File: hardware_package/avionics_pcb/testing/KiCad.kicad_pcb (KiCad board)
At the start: 2 copper layers, 13.3 x 14.6 mm, 4 parts, among them J1 Conn_01x04, U1 AD8603

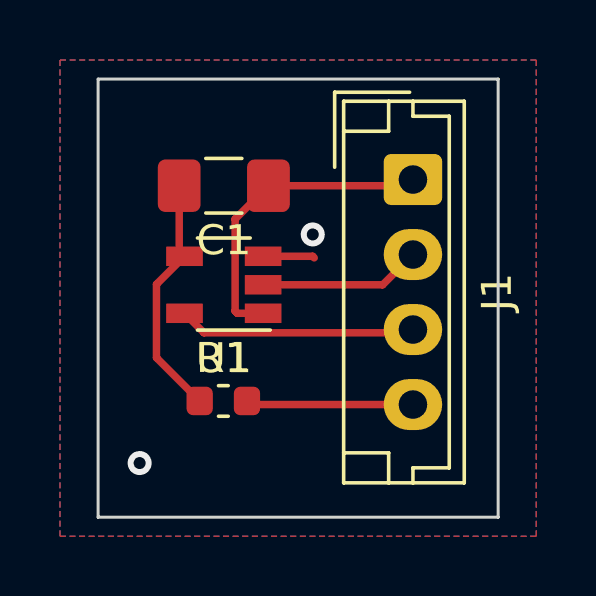
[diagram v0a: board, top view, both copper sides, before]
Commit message: disconnected pad from PCB, testing if the pipeline works correctly
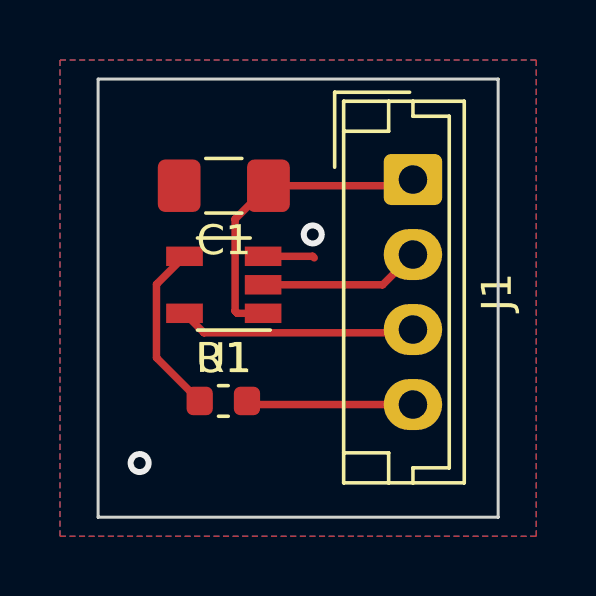
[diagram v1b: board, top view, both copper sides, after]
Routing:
- net Net-(C1-Pad2): track 8.23 -> 6.06 mm

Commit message: Connected pad to PCB, testing if the pipeline works correctly
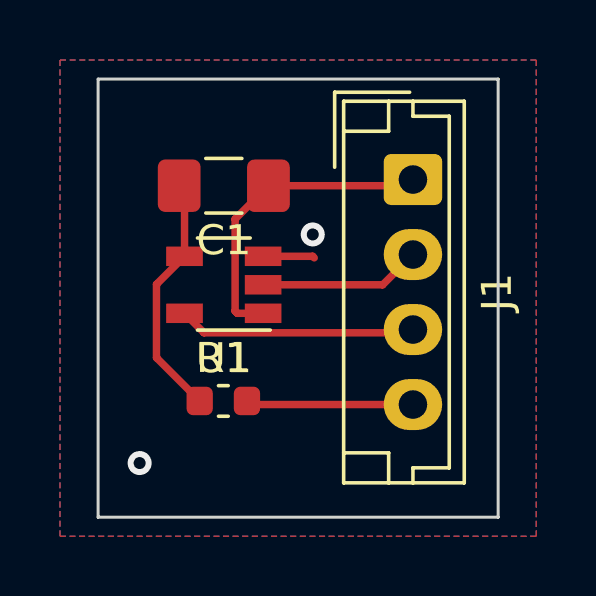
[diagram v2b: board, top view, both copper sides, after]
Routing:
- net Net-(C1-Pad2): track 6.06 -> 8.48 mm
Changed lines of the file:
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@@
     (thickness 1.6)
     (drawings 4)
-    (tracks 22)
+    (tracks 24)
     (zones 0)
     (modules 4)
@@
       (effects (font (size 0.5 0.5) (thickness 0.125)))
     )
+    (fp_line (start -1.6 0.8) (end -1.6 -0.8) (layer F.Fab) (width 0.1))
+    (fp_line (start -1.6 -0.8) (end 1.6 -0.8) (layer F.Fab) (width 0.1))
+    (fp_line (start 1.6 -0.8) (end 1.6 0.8) (layer F.Fab) (width 0.1))
+    (fp_line (start 1.6 0.8) (end -1.6 0.8) (layer F.Fab) (width 0.1))
+    (fp_line (start -0.602064 -0.91) (end 0.602064 -0.91) (layer F.SilkS) (width 0.12))
+    (fp_line (start -0.602064 0.91) (end 0.602064 0.91) (layer F.SilkS) (width 0.12))
+    (fp_line (start -2.45 1.12) (end -2.45 -1.12) (layer F.CrtYd) (width 0.05))
+    (fp_line (start -2.45 -1.12) (end 2.45 -1.12) (layer F.CrtYd) (width 0.05))
+    (fp_line (start 2.45 -1.12) (end 2.45 1.12) (layer F.CrtYd) (width 0.05))
     (fp_line (start 2.45 1.12) (end -2.45 1.12) (layer F.CrtYd) (width 0.05))
-    (fp_line (start 2.45 -1.12) (end 2.45 1.12) (layer F.CrtYd) (width 0.05))
-    (fp_line (start -2.45 -1.12) (end 2.45 -1.12) (layer F.CrtYd) (width 0.05))
-    (fp_line (start -2.45 1.12) (end -2.45 -1.12) (layer F.CrtYd) (width 0.05))
-    (fp_line (start -0.602064 0.91) (end 0.602064 0.91) (layer F.SilkS) (width 0.12))
-    (fp_line (start -0.602064 -0.91) (end 0.602064 -0.91) (layer F.SilkS) (width 0.12))
-    (fp_line (start 1.6 0.8) (end -1.6 0.8) (layer F.Fab) (width 0.1))
-    (fp_line (start 1.6 -0.8) (end 1.6 0.8) (layer F.Fab) (width 0.1))
-    (fp_line (start -1.6 -0.8) (end 1.6 -0.8) (layer F.Fab) (width 0.1))
-    (fp_line (start -1.6 0.8) (end -1.6 -0.8) (layer F.Fab) (width 0.1))
     (fp_text user %R (at 0 0) (layer F.Fab)
       (effects (font (size 0.8 0.8) (thickness 0.12)))
@@
       (effects (font (size 0.5 0.5) (thickness 0.125)))
     )
+    (fp_line (start -0.8 0.4) (end -0.8 -0.4) (layer F.Fab) (width 0.1))
+    (fp_line (start -0.8 -0.4) (end 0.8 -0.4) (layer F.Fab) (width 0.1))
+    (fp_line (start 0.8 -0.4) (end 0.8 0.4) (layer F.Fab) (width 0.1))
+    (fp_line (start 0.8 0.4) (end -0.8 0.4) (layer F.Fab) (width 0.1))
+    (fp_line (start -0.162779 -0.51) (end 0.162779 -0.51) (layer F.SilkS) (width 0.12))
+    (fp_line (start -0.162779 0.51) (end 0.162779 0.51) (layer F.SilkS) (width 0.12))
+    (fp_line (start -1.48 0.73) (end -1.48 -0.73) (layer F.CrtYd) (width 0.05))
+    (fp_line (start -1.48 -0.73) (end 1.48 -0.73) (layer F.CrtYd) (width 0.05))
+    (fp_line (start 1.48 -0.73) (end 1.48 0.73) (layer F.CrtYd) (width 0.05))
     (fp_line (start 1.48 0.73) (end -1.48 0.73) (layer F.CrtYd) (width 0.05))
-    (fp_line (start 1.48 -0.73) (end 1.48 0.73) (layer F.CrtYd) (width 0.05))
-    (fp_line (start -1.48 -0.73) (end 1.48 -0.73) (layer F.CrtYd) (width 0.05))
-    (fp_line (start -1.48 0.73) (end -1.48 -0.73) (layer F.CrtYd) (width 0.05))
-    (fp_line (start -0.162779 0.51) (end 0.162779 0.51) (layer F.SilkS) (width 0.12))
-    (fp_line (start -0.162779 -0.51) (end 0.162779 -0.51) (layer F.SilkS) (width 0.12))
-    (fp_line (start 0.8 0.4) (end -0.8 0.4) (layer F.Fab) (width 0.1))
-    (fp_line (start 0.8 -0.4) (end 0.8 0.4) (layer F.Fab) (width 0.1))
-    (fp_line (start -0.8 -0.4) (end 0.8 -0.4) (layer F.Fab) (width 0.1))
-    (fp_line (start -0.8 0.4) (end -0.8 -0.4) (layer F.Fab) (width 0.1))
     (fp_text user %R (at 0 0) (layer F.Fab)
       (effects (font (size 0.4 0.4) (thickness 0.06)))
@@
       (effects (font (size 0.5 0.5) (thickness 0.125)))
     )
+    (fp_line (start -0.88 1.56) (end 0.88 1.56) (layer F.SilkS) (width 0.12))
+    (fp_line (start 0.88 -1.51) (end -1.55 -1.51) (layer F.SilkS) (width 0.12))
+    (fp_line (start -0.88 -1) (end -0.43 -1.45) (layer F.Fab) (width 0.1))
+    (fp_line (start 0.88 -1.45) (end -0.43 -1.45) (layer F.Fab) (width 0.1))
+    (fp_line (start -0.88 -1) (end -0.88 1.45) (layer F.Fab) (width 0.1))
+    (fp_line (start 0.88 1.45) (end -0.88 1.45) (layer F.Fab) (width 0.1))
+    (fp_line (start 0.88 -1.45) (end 0.88 1.45) (layer F.Fab) (width 0.1))
+    (fp_line (start -2.17 -1.7) (end 2.17 -1.7) (layer F.CrtYd) (width 0.05))
+    (fp_line (start -2.17 -1.7) (end -2.17 1.7) (layer F.CrtYd) (width 0.05))
+    (fp_line (start 2.17 1.7) (end 2.17 -1.7) (layer F.CrtYd) (width 0.05))
     (fp_line (start 2.17 1.7) (end -2.17 1.7) (layer F.CrtYd) (width 0.05))
-    (fp_line (start 2.17 1.7) (end 2.17 -1.7) (layer F.CrtYd) (width 0.05))
-    (fp_line (start -2.17 -1.7) (end -2.17 1.7) (layer F.CrtYd) (width 0.05))
-    (fp_line (start -2.17 -1.7) (end 2.17 -1.7) (layer F.CrtYd) (width 0.05))
-    (fp_line (start 0.88 -1.45) (end 0.88 1.45) (layer F.Fab) (width 0.1))
-    (fp_line (start 0.88 1.45) (end -0.88 1.45) (layer F.Fab) (width 0.1))
-    (fp_line (start -0.88 -1) (end -0.88 1.45) (layer F.Fab) (width 0.1))
-    (fp_line (start 0.88 -1.45) (end -0.43 -1.45) (layer F.Fab) (width 0.1))
-    (fp_line (start -0.88 -1) (end -0.43 -1.45) (layer F.Fab) (width 0.1))
-    (fp_line (start 0.88 -1.51) (end -1.55 -1.51) (layer F.SilkS) (width 0.12))
-    (fp_line (start -0.88 1.56) (end 0.88 1.56) (layer F.SilkS) (width 0.12))
     (fp_text user %R (at 0 0) (layer F.Fab)
       (effects (font (size 0.5 0.5) (thickness 0.075)))
@@
       (effects (font (size 1 1) (thickness 0.15)))
     )
+    (fp_line (start -2.91 2.61) (end -0.41 2.61) (layer F.Fab) (width 0.1))
+    (fp_line (start -2.91 0.11) (end -2.91 2.61) (layer F.Fab) (width 0.1))
+    (fp_line (start -2.91 2.61) (end -0.41 2.61) (layer F.SilkS) (width 0.12))
+    (fp_line (start -2.91 0.11) (end -2.91 2.61) (layer F.SilkS) (width 0.12))
+    (fp_line (start 9.11 0.81) (end 9.11 2.31) (layer F.SilkS) (width 0.12))
+    (fp_line (start 10.11 0.81) (end 9.11 0.81) (layer F.SilkS) (width 0.12))
+    (fp_line (start -1.61 0.81) (end -1.61 2.31) (layer F.SilkS) (width 0.12))
+    (fp_line (start -2.61 0.81) (end -1.61 0.81) (layer F.SilkS) (width 0.12))
+    (fp_line (start 9.61 0) (end 10.11 0) (layer F.SilkS) (width 0.12))
+    (fp_line (start 9.61 -1.21) (end 9.61 0) (layer F.SilkS) (width 0.12))
+    (fp_line (start -2.11 -1.21) (end 9.61 -1.21) (layer F.SilkS) (width 0.12))
+    (fp_line (start -2.11 0) (end -2.11 -1.21) (layer F.SilkS) (width 0.12))
+    (fp_line (start -2.61 0) (end -2.11 0) (layer F.SilkS) (width 0.12))
+    (fp_line (start 10.11 -1.71) (end -2.61 -1.71) (layer F.SilkS) (width 0.12))
+    (fp_line (start 10.11 2.31) (end 10.11 -1.71) (layer F.SilkS) (width 0.12))
+    (fp_line (start -2.61 2.31) (end 10.11 2.31) (layer F.SilkS) (width 0.12))
+    (fp_line (start -2.61 -1.71) (end -2.61 2.31) (layer F.SilkS) (width 0.12))
+    (fp_line (start 10.5 -2.1) (end -3 -2.1) (layer F.CrtYd) (width 0.05))
+    (fp_line (start 10.5 2.7) (end 10.5 -2.1) (layer F.CrtYd) (width 0.05))
+    (fp_line (start -3 2.7) (end 10.5 2.7) (layer F.CrtYd) (width 0.05))
+    (fp_line (start -3 -2.1) (end -3 2.7) (layer F.CrtYd) (width 0.05))
+    (fp_line (start 10 -1.6) (end -2.5 -1.6) (layer F.Fab) (width 0.1))
+    (fp_line (start 10 2.2) (end 10 -1.6) (layer F.Fab) (width 0.1))
+    (fp_line (start -2.5 2.2) (end 10 2.2) (layer F.Fab) (width 0.1))
     (fp_line (start -2.5 -1.6) (end -2.5 2.2) (layer F.Fab) (width 0.1))
-    (fp_line (start -2.5 2.2) (end 10 2.2) (layer F.Fab) (width 0.1))
-    (fp_line (start 10 2.2) (end 10 -1.6) (layer F.Fab) (width 0.1))
-    (fp_line (start 10 -1.6) (end -2.5 -1.6) (layer F.Fab) (width 0.1))
-    (fp_line (start -3 -2.1) (end -3 2.7) (layer F.CrtYd) (width 0.05))
-    (fp_line (start -3 2.7) (end 10.5 2.7) (layer F.CrtYd) (width 0.05))
-    (fp_line (start 10.5 2.7) (end 10.5 -2.1) (layer F.CrtYd) (width 0.05))
-    (fp_line (start 10.5 -2.1) (end -3 -2.1) (layer F.CrtYd) (width 0.05))
-    (fp_line (start -2.61 -1.71) (end -2.61 2.31) (layer F.SilkS) (width 0.12))
-    (fp_line (start -2.61 2.31) (end 10.11 2.31) (layer F.SilkS) (width 0.12))
-    (fp_line (start 10.11 2.31) (end 10.11 -1.71) (layer F.SilkS) (width 0.12))
-    (fp_line (start 10.11 -1.71) (end -2.61 -1.71) (layer F.SilkS) (width 0.12))
-    (fp_line (start -2.61 0) (end -2.11 0) (layer F.SilkS) (width 0.12))
-    (fp_line (start -2.11 0) (end -2.11 -1.21) (layer F.SilkS) (width 0.12))
-    (fp_line (start -2.11 -1.21) (end 9.61 -1.21) (layer F.SilkS) (width 0.12))
-    (fp_line (start 9.61 -1.21) (end 9.61 0) (layer F.SilkS) (width 0.12))
-    (fp_line (start 9.61 0) (end 10.11 0) (layer F.SilkS) (width 0.12))
-    (fp_line (start -2.61 0.81) (end -1.61 0.81) (layer F.SilkS) (width 0.12))
-    (fp_line (start -1.61 0.81) (end -1.61 2.31) (layer F.SilkS) (width 0.12))
-    (fp_line (start 10.11 0.81) (end 9.11 0.81) (layer F.SilkS) (width 0.12))
-    (fp_line (start 9.11 0.81) (end 9.11 2.31) (layer F.SilkS) (width 0.12))
-    (fp_line (start -2.91 0.11) (end -2.91 2.61) (layer F.SilkS) (width 0.12))
-    (fp_line (start -2.91 2.61) (end -0.41 2.61) (layer F.SilkS) (width 0.12))
-    (fp_line (start -2.91 0.11) (end -2.91 2.61) (layer F.Fab) (width 0.1))
-    (fp_line (start -2.91 2.61) (end -0.41 2.61) (layer F.Fab) (width 0.1))
     (fp_text user %R (at 3.75 1.5 90) (layer F.Fab)
       (effects (font (size 1 1) (thickness 0.15)))
@@
   (segment (start 94.020999 42.403001) (end 94.020999 44.848499) (width 0.25) (layer F.Cu) (net 2))
   (segment (start 94.956 41.468) (end 94.020999 42.403001) (width 0.25) (layer F.Cu) (net 2))
+  (segment (start 94.956 39.2935) (end 94.7785 39.116) (width 0.25) (layer F.Cu) (net 2))
+  (segment (start 94.956 41.468) (end 94.956 39.2935) (width 0.25) (layer F.Cu) (net 2))
   (segment (start 97.1575 46.41) (end 97.0375 46.29) (width 0.25) (layer F.Cu) (net 3))
   (segment (start 102.57 46.41) (end 97.1575 46.41) (width 0.25) (layer F.Cu) (net 3))

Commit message: testing my own runner
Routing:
- net Net-(C1-Pad2): track 8.48 -> 6.31 mm
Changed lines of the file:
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@@
     (thickness 1.6)
     (drawings 4)
-    (tracks 24)
+    (tracks 23)
     (zones 0)
     (modules 4)
@@
       (effects (font (size 0.5 0.5) (thickness 0.125)))
     )
+    (fp_line (start 2.45 1.12) (end -2.45 1.12) (layer F.CrtYd) (width 0.05))
+    (fp_line (start 2.45 -1.12) (end 2.45 1.12) (layer F.CrtYd) (width 0.05))
+    (fp_line (start -2.45 -1.12) (end 2.45 -1.12) (layer F.CrtYd) (width 0.05))
+    (fp_line (start -2.45 1.12) (end -2.45 -1.12) (layer F.CrtYd) (width 0.05))
+    (fp_line (start -0.602064 0.91) (end 0.602064 0.91) (layer F.SilkS) (width 0.12))
+    (fp_line (start -0.602064 -0.91) (end 0.602064 -0.91) (layer F.SilkS) (width 0.12))
+    (fp_line (start 1.6 0.8) (end -1.6 0.8) (layer F.Fab) (width 0.1))
+    (fp_line (start 1.6 -0.8) (end 1.6 0.8) (layer F.Fab) (width 0.1))
+    (fp_line (start -1.6 -0.8) (end 1.6 -0.8) (layer F.Fab) (width 0.1))
     (fp_line (start -1.6 0.8) (end -1.6 -0.8) (layer F.Fab) (width 0.1))
-    (fp_line (start -1.6 -0.8) (end 1.6 -0.8) (layer F.Fab) (width 0.1))
-    (fp_line (start 1.6 -0.8) (end 1.6 0.8) (layer F.Fab) (width 0.1))
-    (fp_line (start 1.6 0.8) (end -1.6 0.8) (layer F.Fab) (width 0.1))
-    (fp_line (start -0.602064 -0.91) (end 0.602064 -0.91) (layer F.SilkS) (width 0.12))
-    (fp_line (start -0.602064 0.91) (end 0.602064 0.91) (layer F.SilkS) (width 0.12))
-    (fp_line (start -2.45 1.12) (end -2.45 -1.12) (layer F.CrtYd) (width 0.05))
-    (fp_line (start -2.45 -1.12) (end 2.45 -1.12) (layer F.CrtYd) (width 0.05))
-    (fp_line (start 2.45 -1.12) (end 2.45 1.12) (layer F.CrtYd) (width 0.05))
-    (fp_line (start 2.45 1.12) (end -2.45 1.12) (layer F.CrtYd) (width 0.05))
     (fp_text user %R (at 0 0) (layer F.Fab)
       (effects (font (size 0.8 0.8) (thickness 0.12)))
@@
       (effects (font (size 0.5 0.5) (thickness 0.125)))
     )
+    (fp_line (start 1.48 0.73) (end -1.48 0.73) (layer F.CrtYd) (width 0.05))
+    (fp_line (start 1.48 -0.73) (end 1.48 0.73) (layer F.CrtYd) (width 0.05))
+    (fp_line (start -1.48 -0.73) (end 1.48 -0.73) (layer F.CrtYd) (width 0.05))
+    (fp_line (start -1.48 0.73) (end -1.48 -0.73) (layer F.CrtYd) (width 0.05))
+    (fp_line (start -0.162779 0.51) (end 0.162779 0.51) (layer F.SilkS) (width 0.12))
+    (fp_line (start -0.162779 -0.51) (end 0.162779 -0.51) (layer F.SilkS) (width 0.12))
+    (fp_line (start 0.8 0.4) (end -0.8 0.4) (layer F.Fab) (width 0.1))
+    (fp_line (start 0.8 -0.4) (end 0.8 0.4) (layer F.Fab) (width 0.1))
+    (fp_line (start -0.8 -0.4) (end 0.8 -0.4) (layer F.Fab) (width 0.1))
     (fp_line (start -0.8 0.4) (end -0.8 -0.4) (layer F.Fab) (width 0.1))
-    (fp_line (start -0.8 -0.4) (end 0.8 -0.4) (layer F.Fab) (width 0.1))
-    (fp_line (start 0.8 -0.4) (end 0.8 0.4) (layer F.Fab) (width 0.1))
-    (fp_line (start 0.8 0.4) (end -0.8 0.4) (layer F.Fab) (width 0.1))
-    (fp_line (start -0.162779 -0.51) (end 0.162779 -0.51) (layer F.SilkS) (width 0.12))
-    (fp_line (start -0.162779 0.51) (end 0.162779 0.51) (layer F.SilkS) (width 0.12))
-    (fp_line (start -1.48 0.73) (end -1.48 -0.73) (layer F.CrtYd) (width 0.05))
-    (fp_line (start -1.48 -0.73) (end 1.48 -0.73) (layer F.CrtYd) (width 0.05))
-    (fp_line (start 1.48 -0.73) (end 1.48 0.73) (layer F.CrtYd) (width 0.05))
-    (fp_line (start 1.48 0.73) (end -1.48 0.73) (layer F.CrtYd) (width 0.05))
     (fp_text user %R (at 0 0) (layer F.Fab)
       (effects (font (size 0.4 0.4) (thickness 0.06)))
@@
       (effects (font (size 0.5 0.5) (thickness 0.125)))
     )
+    (fp_line (start 2.17 1.7) (end -2.17 1.7) (layer F.CrtYd) (width 0.05))
+    (fp_line (start 2.17 1.7) (end 2.17 -1.7) (layer F.CrtYd) (width 0.05))
+    (fp_line (start -2.17 -1.7) (end -2.17 1.7) (layer F.CrtYd) (width 0.05))
+    (fp_line (start -2.17 -1.7) (end 2.17 -1.7) (layer F.CrtYd) (width 0.05))
+    (fp_line (start 0.88 -1.45) (end 0.88 1.45) (layer F.Fab) (width 0.1))
+    (fp_line (start 0.88 1.45) (end -0.88 1.45) (layer F.Fab) (width 0.1))
+    (fp_line (start -0.88 -1) (end -0.88 1.45) (layer F.Fab) (width 0.1))
+    (fp_line (start 0.88 -1.45) (end -0.43 -1.45) (layer F.Fab) (width 0.1))
+    (fp_line (start -0.88 -1) (end -0.43 -1.45) (layer F.Fab) (width 0.1))
+    (fp_line (start 0.88 -1.51) (end -1.55 -1.51) (layer F.SilkS) (width 0.12))
     (fp_line (start -0.88 1.56) (end 0.88 1.56) (layer F.SilkS) (width 0.12))
-    (fp_line (start 0.88 -1.51) (end -1.55 -1.51) (layer F.SilkS) (width 0.12))
-    (fp_line (start -0.88 -1) (end -0.43 -1.45) (layer F.Fab) (width 0.1))
-    (fp_line (start 0.88 -1.45) (end -0.43 -1.45) (layer F.Fab) (width 0.1))
-    (fp_line (start -0.88 -1) (end -0.88 1.45) (layer F.Fab) (width 0.1))
-    (fp_line (start 0.88 1.45) (end -0.88 1.45) (layer F.Fab) (width 0.1))
-    (fp_line (start 0.88 -1.45) (end 0.88 1.45) (layer F.Fab) (width 0.1))
-    (fp_line (start -2.17 -1.7) (end 2.17 -1.7) (layer F.CrtYd) (width 0.05))
-    (fp_line (start -2.17 -1.7) (end -2.17 1.7) (layer F.CrtYd) (width 0.05))
-    (fp_line (start 2.17 1.7) (end 2.17 -1.7) (layer F.CrtYd) (width 0.05))
-    (fp_line (start 2.17 1.7) (end -2.17 1.7) (layer F.CrtYd) (width 0.05))
     (fp_text user %R (at 0 0) (layer F.Fab)
       (effects (font (size 0.5 0.5) (thickness 0.075)))
@@
       (effects (font (size 1 1) (thickness 0.15)))
     )
+    (fp_line (start -2.5 -1.6) (end -2.5 2.2) (layer F.Fab) (width 0.1))
+    (fp_line (start -2.5 2.2) (end 10 2.2) (layer F.Fab) (width 0.1))
+    (fp_line (start 10 2.2) (end 10 -1.6) (layer F.Fab) (width 0.1))
+    (fp_line (start 10 -1.6) (end -2.5 -1.6) (layer F.Fab) (width 0.1))
+    (fp_line (start -3 -2.1) (end -3 2.7) (layer F.CrtYd) (width 0.05))
+    (fp_line (start -3 2.7) (end 10.5 2.7) (layer F.CrtYd) (width 0.05))
+    (fp_line (start 10.5 2.7) (end 10.5 -2.1) (layer F.CrtYd) (width 0.05))
+    (fp_line (start 10.5 -2.1) (end -3 -2.1) (layer F.CrtYd) (width 0.05))
+    (fp_line (start -2.61 -1.71) (end -2.61 2.31) (layer F.SilkS) (width 0.12))
+    (fp_line (start -2.61 2.31) (end 10.11 2.31) (layer F.SilkS) (width 0.12))
+    (fp_line (start 10.11 2.31) (end 10.11 -1.71) (layer F.SilkS) (width 0.12))
+    (fp_line (start 10.11 -1.71) (end -2.61 -1.71) (layer F.SilkS) (width 0.12))
+    (fp_line (start -2.61 0) (end -2.11 0) (layer F.SilkS) (width 0.12))
+    (fp_line (start -2.11 0) (end -2.11 -1.21) (layer F.SilkS) (width 0.12))
+    (fp_line (start -2.11 -1.21) (end 9.61 -1.21) (layer F.SilkS) (width 0.12))
+    (fp_line (start 9.61 -1.21) (end 9.61 0) (layer F.SilkS) (width 0.12))
+    (fp_line (start 9.61 0) (end 10.11 0) (layer F.SilkS) (width 0.12))
+    (fp_line (start -2.61 0.81) (end -1.61 0.81) (layer F.SilkS) (width 0.12))
+    (fp_line (start -1.61 0.81) (end -1.61 2.31) (layer F.SilkS) (width 0.12))
+    (fp_line (start 10.11 0.81) (end 9.11 0.81) (layer F.SilkS) (width 0.12))
+    (fp_line (start 9.11 0.81) (end 9.11 2.31) (layer F.SilkS) (width 0.12))
+    (fp_line (start -2.91 0.11) (end -2.91 2.61) (layer F.SilkS) (width 0.12))
+    (fp_line (start -2.91 2.61) (end -0.41 2.61) (layer F.SilkS) (width 0.12))
+    (fp_line (start -2.91 0.11) (end -2.91 2.61) (layer F.Fab) (width 0.1))
     (fp_line (start -2.91 2.61) (end -0.41 2.61) (layer F.Fab) (width 0.1))
-    (fp_line (start -2.91 0.11) (end -2.91 2.61) (layer F.Fab) (width 0.1))
-    (fp_line (start -2.91 2.61) (end -0.41 2.61) (layer F.SilkS) (width 0.12))
-    (fp_line (start -2.91 0.11) (end -2.91 2.61) (layer F.SilkS) (width 0.12))
-    (fp_line (start 9.11 0.81) (end 9.11 2.31) (layer F.SilkS) (width 0.12))
-    (fp_line (start 10.11 0.81) (end 9.11 0.81) (layer F.SilkS) (width 0.12))
-    (fp_line (start -1.61 0.81) (end -1.61 2.31) (layer F.SilkS) (width 0.12))
-    (fp_line (start -2.61 0.81) (end -1.61 0.81) (layer F.SilkS) (width 0.12))
-    (fp_line (start 9.61 0) (end 10.11 0) (layer F.SilkS) (width 0.12))
-    (fp_line (start 9.61 -1.21) (end 9.61 0) (layer F.SilkS) (width 0.12))
-    (fp_line (start -2.11 -1.21) (end 9.61 -1.21) (layer F.SilkS) (width 0.12))
-    (fp_line (start -2.11 0) (end -2.11 -1.21) (layer F.SilkS) (width 0.12))
-    (fp_line (start -2.61 0) (end -2.11 0) (layer F.SilkS) (width 0.12))
-    (fp_line (start 10.11 -1.71) (end -2.61 -1.71) (layer F.SilkS) (width 0.12))
-    (fp_line (start 10.11 2.31) (end 10.11 -1.71) (layer F.SilkS) (width 0.12))
-    (fp_line (start -2.61 2.31) (end 10.11 2.31) (layer F.SilkS) (width 0.12))
-    (fp_line (start -2.61 -1.71) (end -2.61 2.31) (layer F.SilkS) (width 0.12))
-    (fp_line (start 10.5 -2.1) (end -3 -2.1) (layer F.CrtYd) (width 0.05))
-    (fp_line (start 10.5 2.7) (end 10.5 -2.1) (layer F.CrtYd) (width 0.05))
-    (fp_line (start -3 2.7) (end 10.5 2.7) (layer F.CrtYd) (width 0.05))
-    (fp_line (start -3 -2.1) (end -3 2.7) (layer F.CrtYd) (width 0.05))
-    (fp_line (start 10 -1.6) (end -2.5 -1.6) (layer F.Fab) (width 0.1))
-    (fp_line (start 10 2.2) (end 10 -1.6) (layer F.Fab) (width 0.1))
-    (fp_line (start -2.5 2.2) (end 10 2.2) (layer F.Fab) (width 0.1))
-    (fp_line (start -2.5 -1.6) (end -2.5 2.2) (layer F.Fab) (width 0.1))
     (fp_text user %R (at 3.75 1.5 90) (layer F.Fab)
       (effects (font (size 1 1) (thickness 0.15)))
@@
   (segment (start 94.956 41.468) (end 94.020999 42.403001) (width 0.25) (layer F.Cu) (net 2))
   (segment (start 94.956 39.2935) (end 94.7785 39.116) (width 0.25) (layer F.Cu) (net 2))
-  (segment (start 94.956 41.468) (end 94.956 39.2935) (width 0.25) (layer F.Cu) (net 2))
   (segment (start 97.1575 46.41) (end 97.0375 46.29) (width 0.25) (layer F.Cu) (net 3))
   (segment (start 102.57 46.41) (end 97.1575 46.41) (width 0.25) (layer F.Cu) (net 3))
